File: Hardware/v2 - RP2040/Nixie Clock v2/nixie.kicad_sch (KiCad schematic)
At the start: 18 parts, among them Q1 PZTA92, Q2 MMBTA42, U3 К155ИД1, U4 К155ИД1, U5 К155ИД1, U6 К155ИД1, U7 NCH8200HV

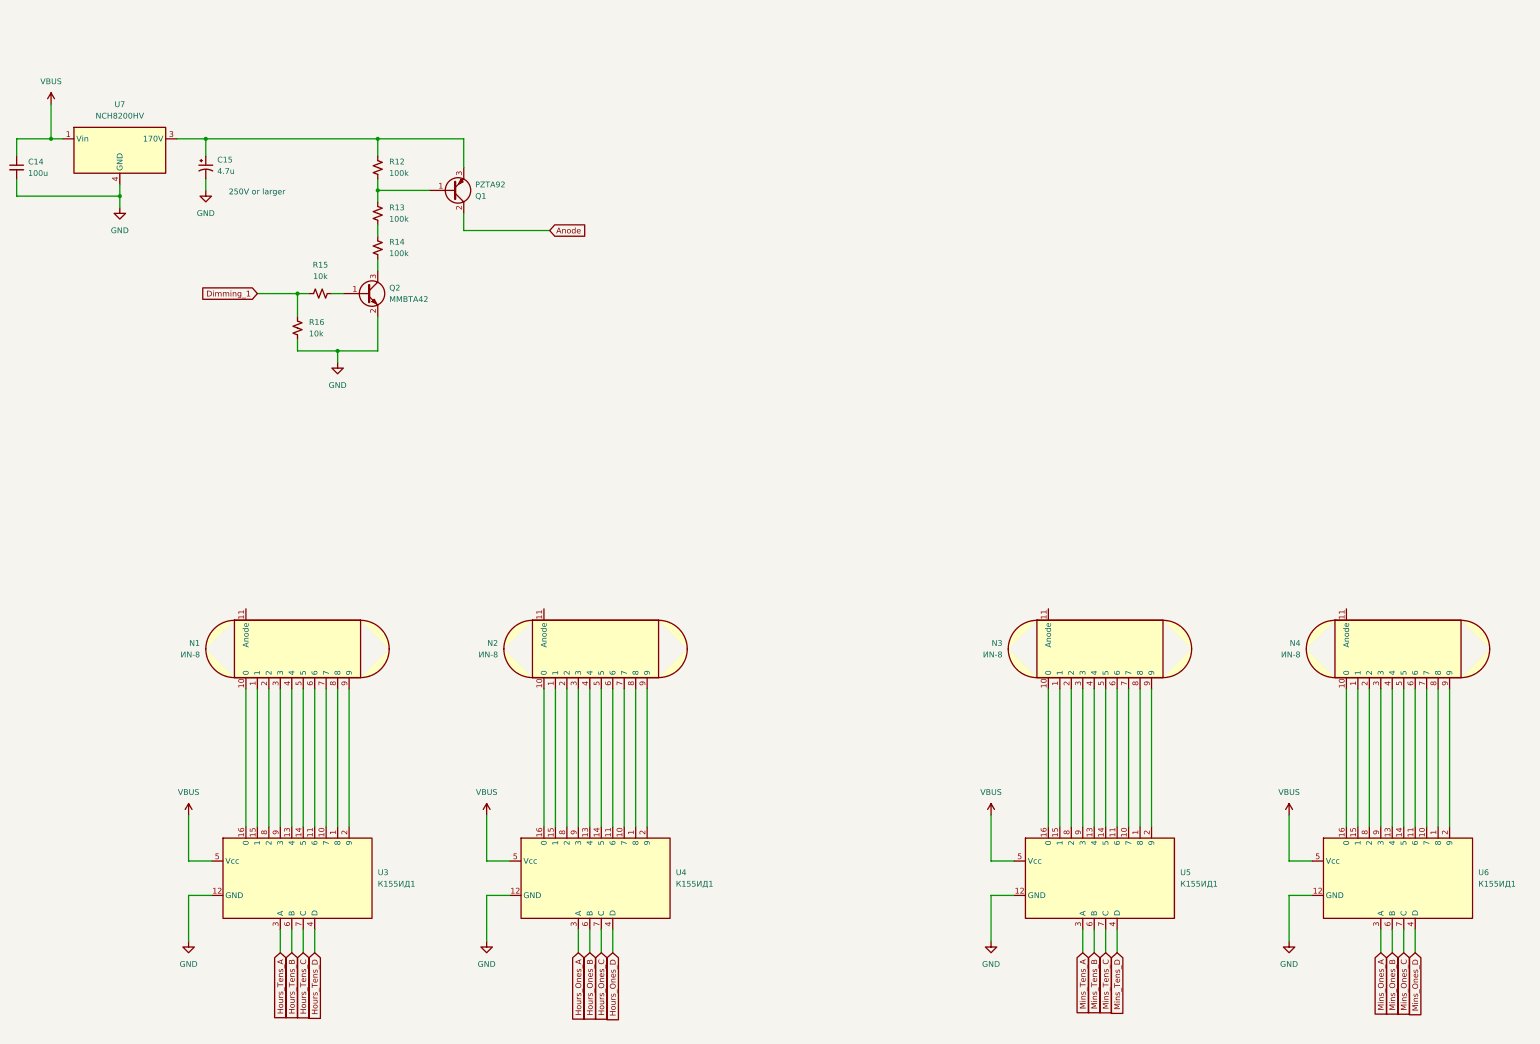
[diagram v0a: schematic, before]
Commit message: Complteted schematic, mergerd schematic on to one sheet, started assigning footprints
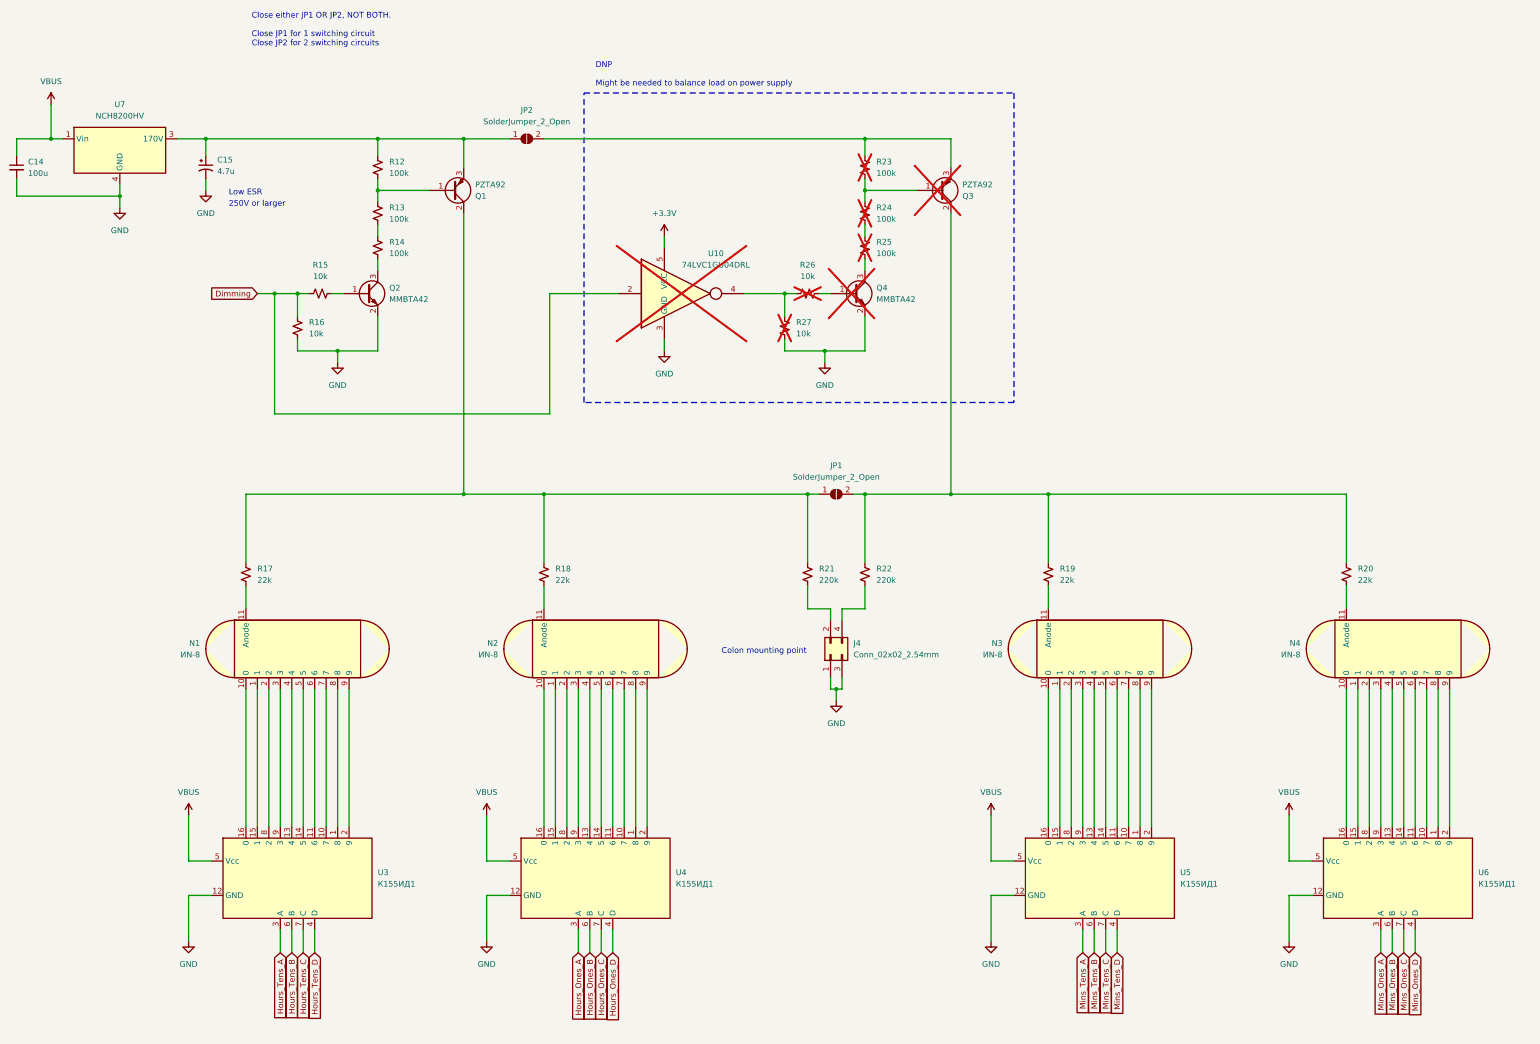
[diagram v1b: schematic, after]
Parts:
- added J4: Conn_02x02_2.54mm, symbol Connector_Generic:Conn_02x02_Odd_Even
- added JP1, JP2: SolderJumper_2_Open, symbol Jumper:SolderJumper_2_Open
- added Q3: PZTA92, Package_TO_SOT_SMD:SOT-223-3_TabPin2, symbol Transistor_BJT:PZTA92
- added Q4: MMBTA42, Package_TO_SOT_SMD:SOT-23, symbol Transistor_BJT:MMBTA42
- added R17, R18, R19, R20: 22k, symbol Device:R_Small_US
- added R21, R22: 220k, symbol Device:R_Small_US
- added R23, R24, R25: 100k, symbol Device:R_Small_US
- added R26, R27: 10k, symbol Device:R_Small_US
- added U10: 74LVC1GU04DRL, Package_TO_SOT_SMD:SOT-553, symbol 74xGxx:74LVC1GU04DRL
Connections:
- net GND: now also J4.1 (Pin_1), J4.3 (Pin_3), Q4.2 (E), R27.2, U10.3 (GND)
- net at N3.11 (Anode): now also R19.2
- net at C15.1, Q1.3 (E), R12.1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: now also JP2.1 (A)
- net at N4.11 (Anode): now also R20.2
- net at N2.11 (Anode): now also R18.2
- net at N1.11 (Anode): now also R17.2
- net Anode: no longer names the net of Q1.2 (C)
- net Anode: now also JP1.1 (A), R17.1, R18.1, R21.1
- net Dimming_1 renamed Dimming
- net Dimming: now also U10.2
- new net: Q3.1 (B), R23.2, R24.1
- new net: JP1.2 (B), Q3.2 (C), R19.1, R20.1, R22.1
- new net: JP2.2 (B), Q3.3 (E), R23.1
- new net: R26.1, R27.1, U10.4
- new net: Q4.1 (B), R26.2
- new net: Q4.3 (C), R25.2
- new net: J4.2 (Pin_2), R21.2
- new net: J4.4 (Pin_4), R22.2
- new net: R24.2, R25.1
- new net +3.3V: U10.5 (VCC)
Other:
- note added: "Close either JP1 OR JP2, NOT BOTH. Close JP1 for 1 switching circuit Close JP2 for 2 switching circuits"
- note added: "Colon mounting point"
- note added: "DNP Might be needed to balance load on power supply"
- note added: "Low ESR"
